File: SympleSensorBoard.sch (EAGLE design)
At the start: 49 parts, among them IC1 STM32F303K8T6, J1 B2B-XH-A_LF__SN_, J10 B3B-XH-A_LF__SN_, J11 B3B-XH-A_LF__SN_, J12 B4B-XH-A_LF__SN_, J13 B4B-XH-A_LF__SN_, J14 B4B-XH-A_LF__SN_, J15 B4B-XH-A_LF__SN_, J16 B2B-XH-A_LF__SN_, J2 B2B-XH-A_LF__SN_, J3 B2B-XH-A_LF__SN_, J4 B2B-XH-A_LF__SN_, J5 B2B-XH-A_LF__SN_, J6 B3B-XH-A_LF__SN_, J7 B3B-XH-A_LF__SN_, J8 B3B-XH-A_LF__SN_, J9 B3B-XH-A_LF__SN_, Y1 CSTCE12M0G55-R0

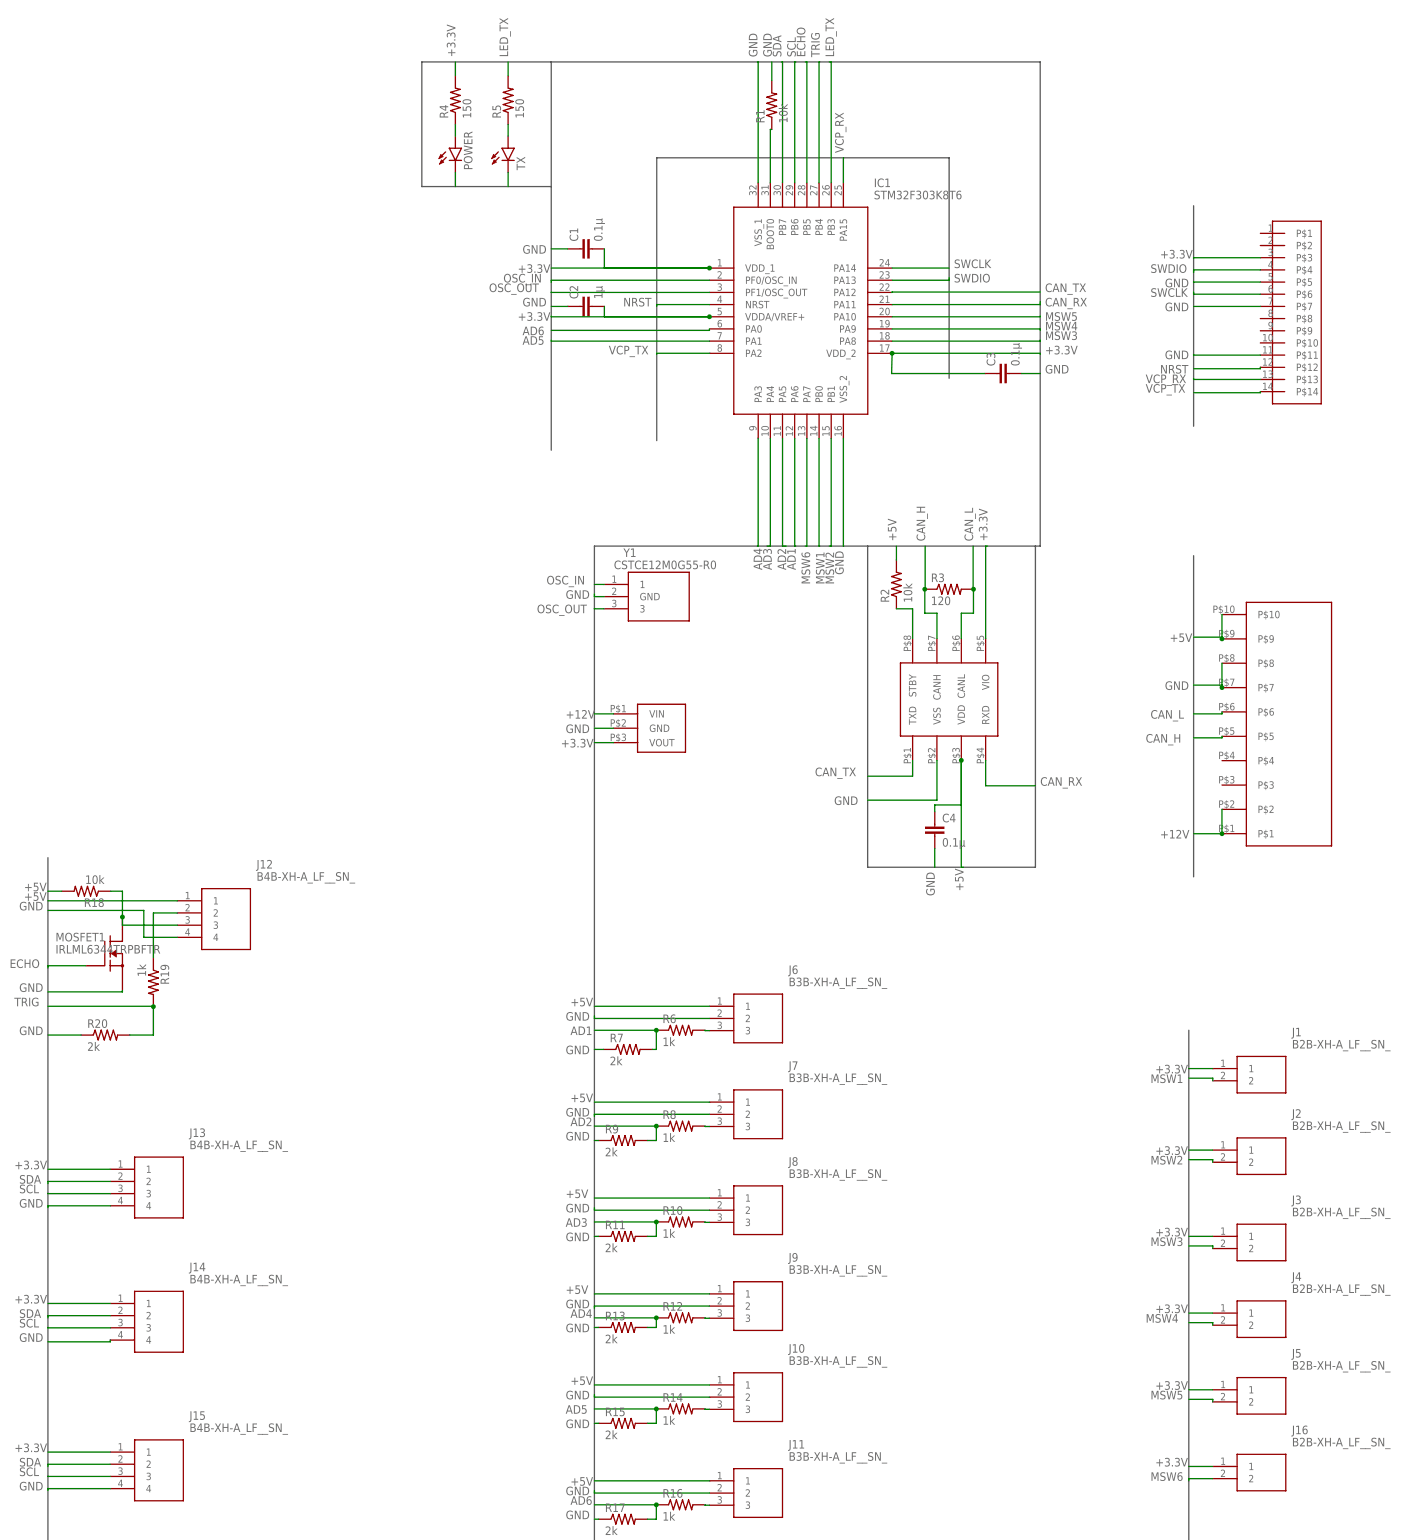
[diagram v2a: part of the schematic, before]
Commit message: コネクタ位置の修正、コネクタ番号を基盤上に表示、部品の再配置、再配線完了。使うセンサはまだ決まっていない。
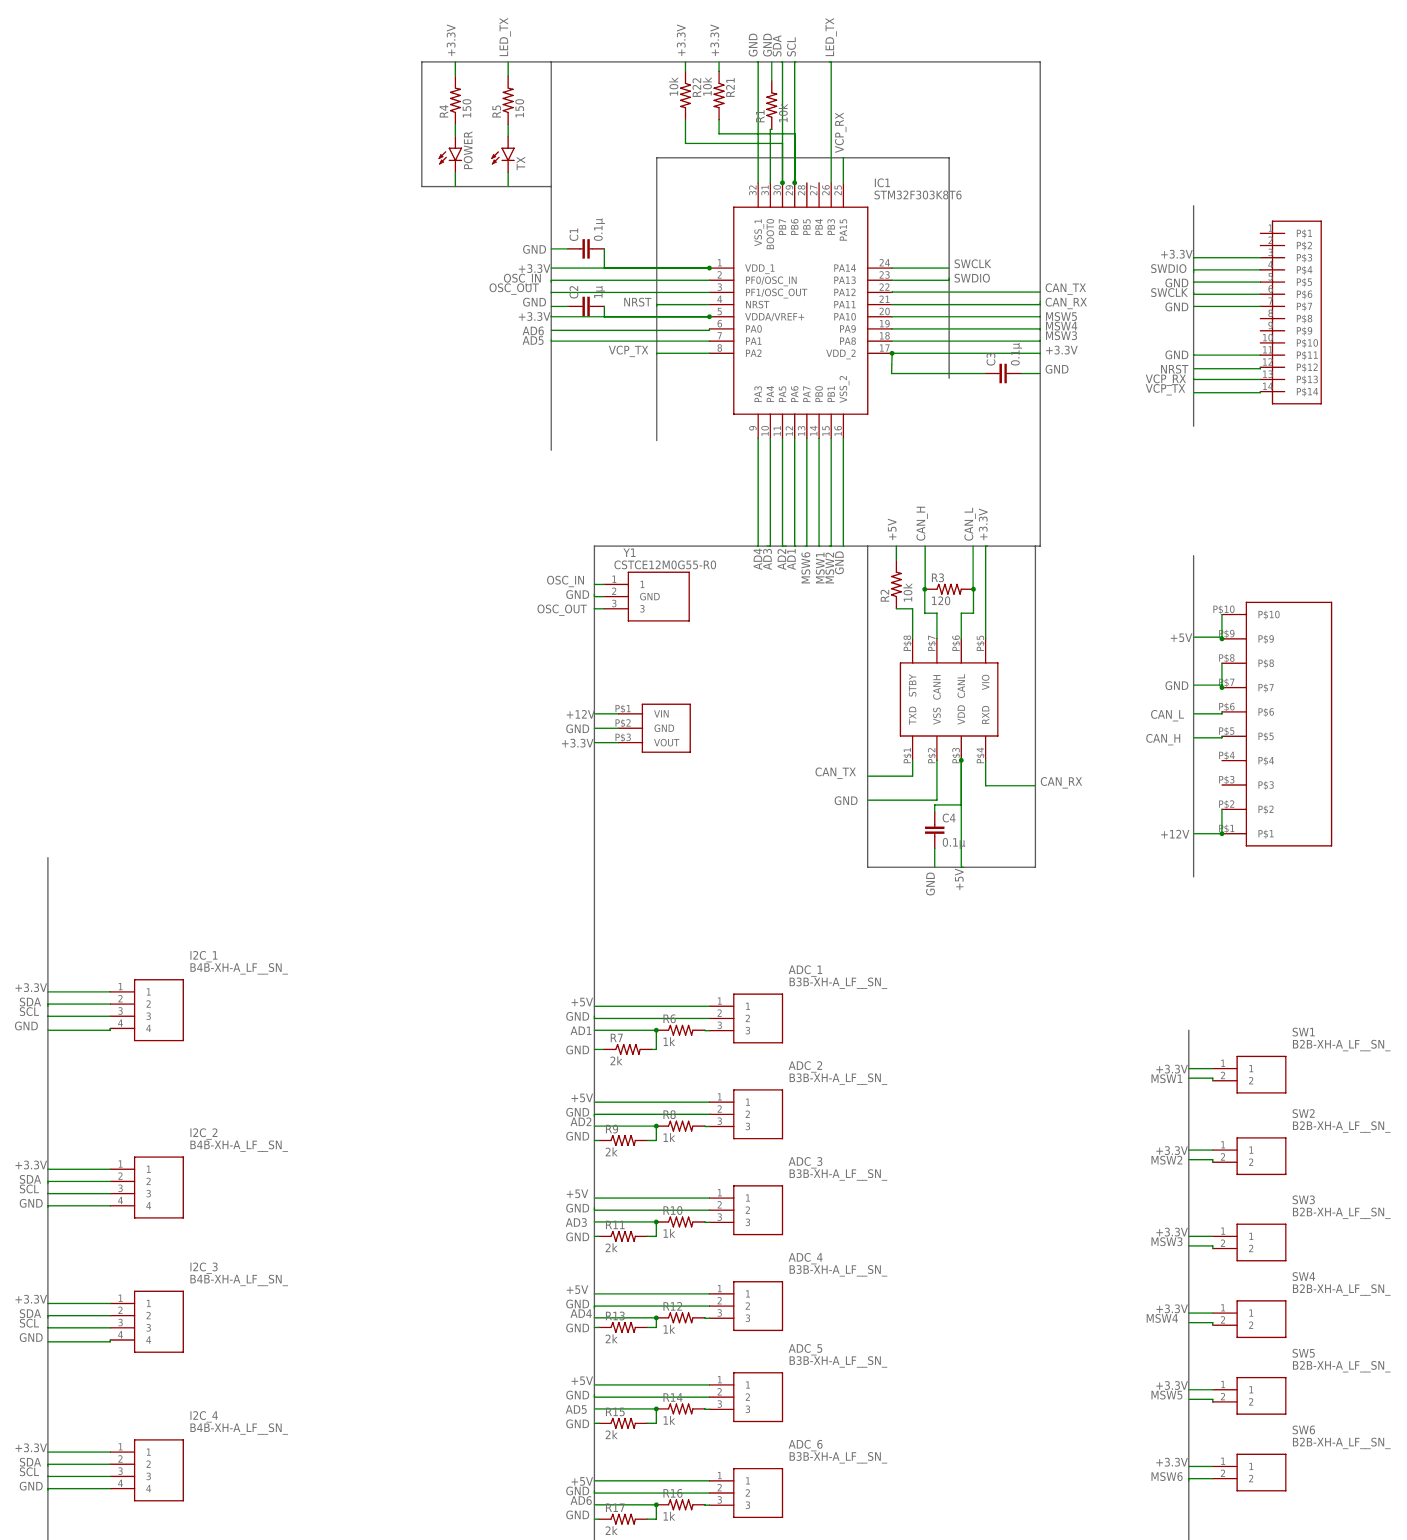
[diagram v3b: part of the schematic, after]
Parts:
- removed J12: B4B-XH-A_LF__SN_, B4B-XH-A_LF__SN_:B4B-XH-A_LF__SN_
- removed MOSFET1: IRLML6344TRPBFTR, mukuchin_transistor_fet_igbt:IRLML6344TRPBFTR
- removed R18: 10k, rcl:R-US_R0603
- removed R19: 1k, rcl:R-US_R0603
- removed R20: 2k, rcl:R-US_R0603
- added I2C_1: B4B-XH-A_LF__SN_, B4B-XH-A_LF__SN_:B4B-XH-A_LF__SN_
- added R21, R22: 10k, rcl:R-US_R0603
- renumbered J1 to SW1, J10 to ADC_5, J11 to ADC_6, J13 to I2C_2, J14 to I2C_3, J15 to I2C_4, J16 to SW6, J2 to SW2, J3 to SW3, J4 to SW4, J5 to SW5, J6 to ADC_1, J7 to ADC_2, J8 to ADC_3, J9 to ADC_4
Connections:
- removed net ECHO: IC1.PB5, MOSFET1.G
- removed net N$11: J12.3, MOSFET1.D, R18.1
- removed net N$13: J12.2, R19.1
- removed net TRIG: IC1.PB4, R19.2, R20.2
- net +3.3V: now also I2C_1.1, R21.1, R22.1
- net +5V: no longer J12.1, R18.2
- net GND: now also I2C_1.4; no longer J12.4, MOSFET1.S, R20.1
- net SCL: now also I2C_1.3, R21.2
- net SDA: now also I2C_1.2, R22.2

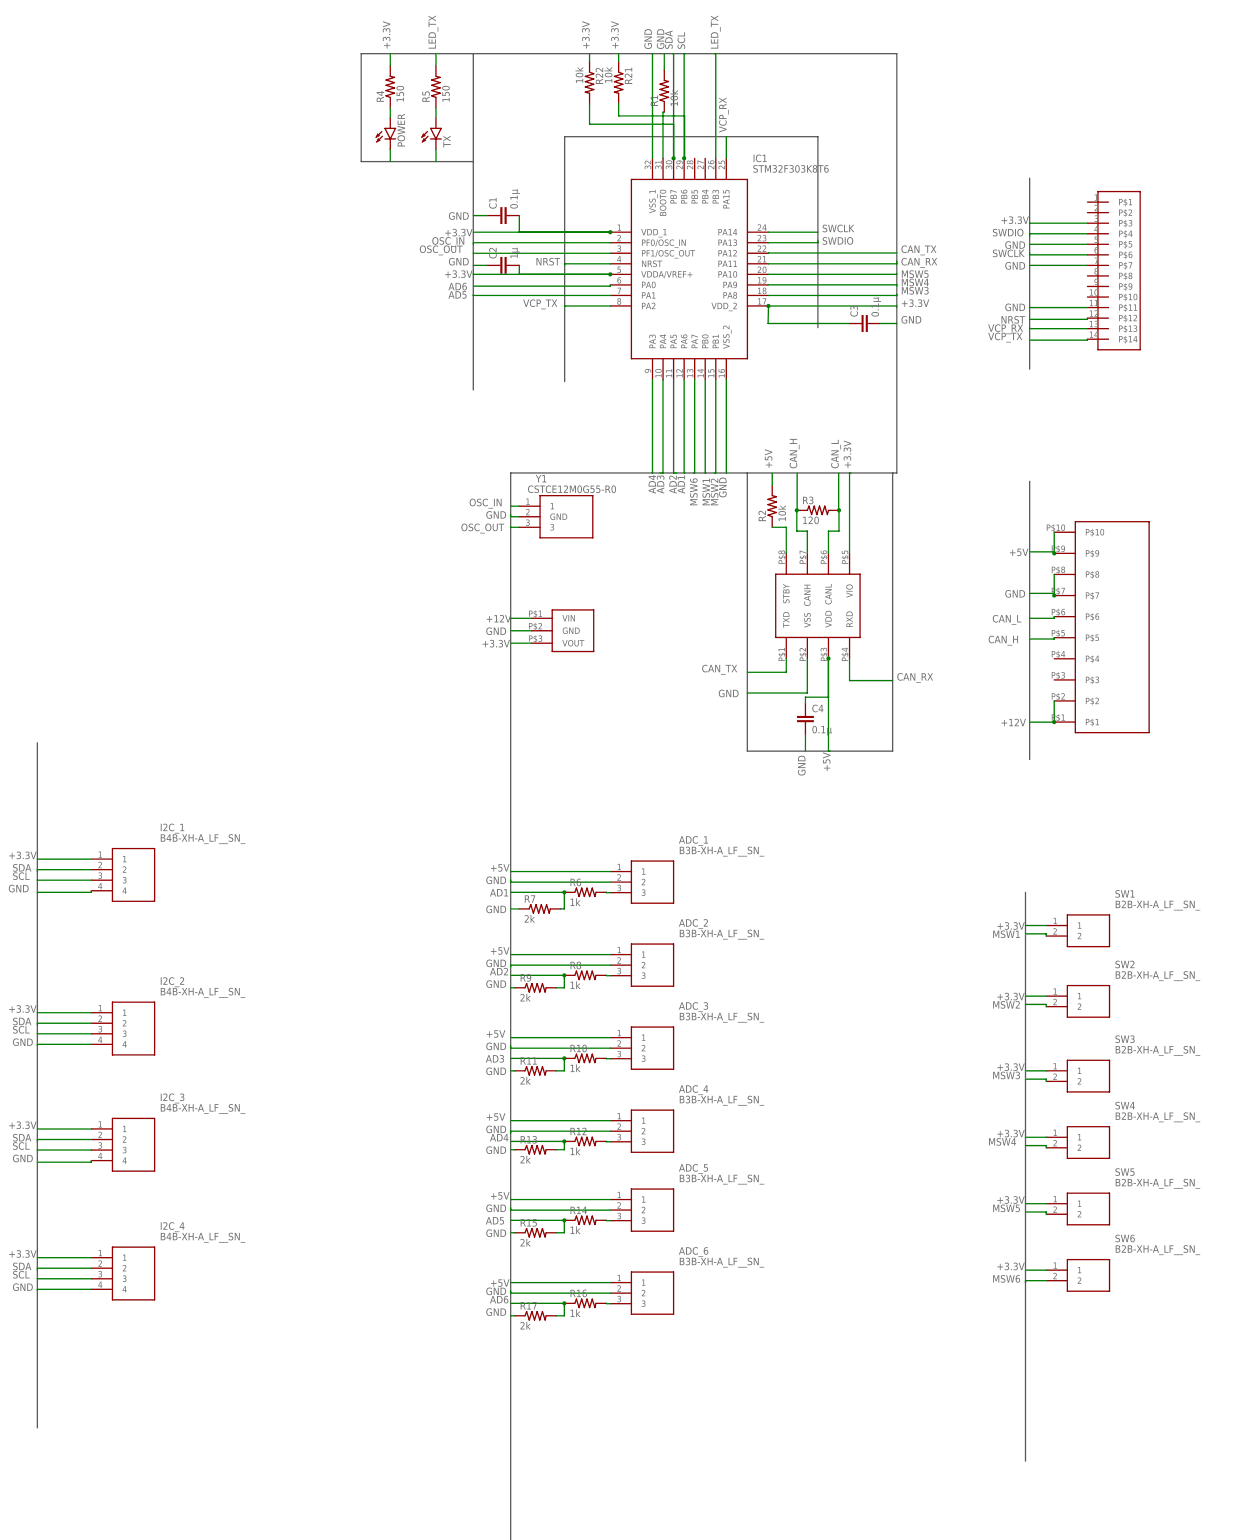
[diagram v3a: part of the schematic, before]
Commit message: I2Cコネクタを全て外した。I2Cは別の基盤で行う。
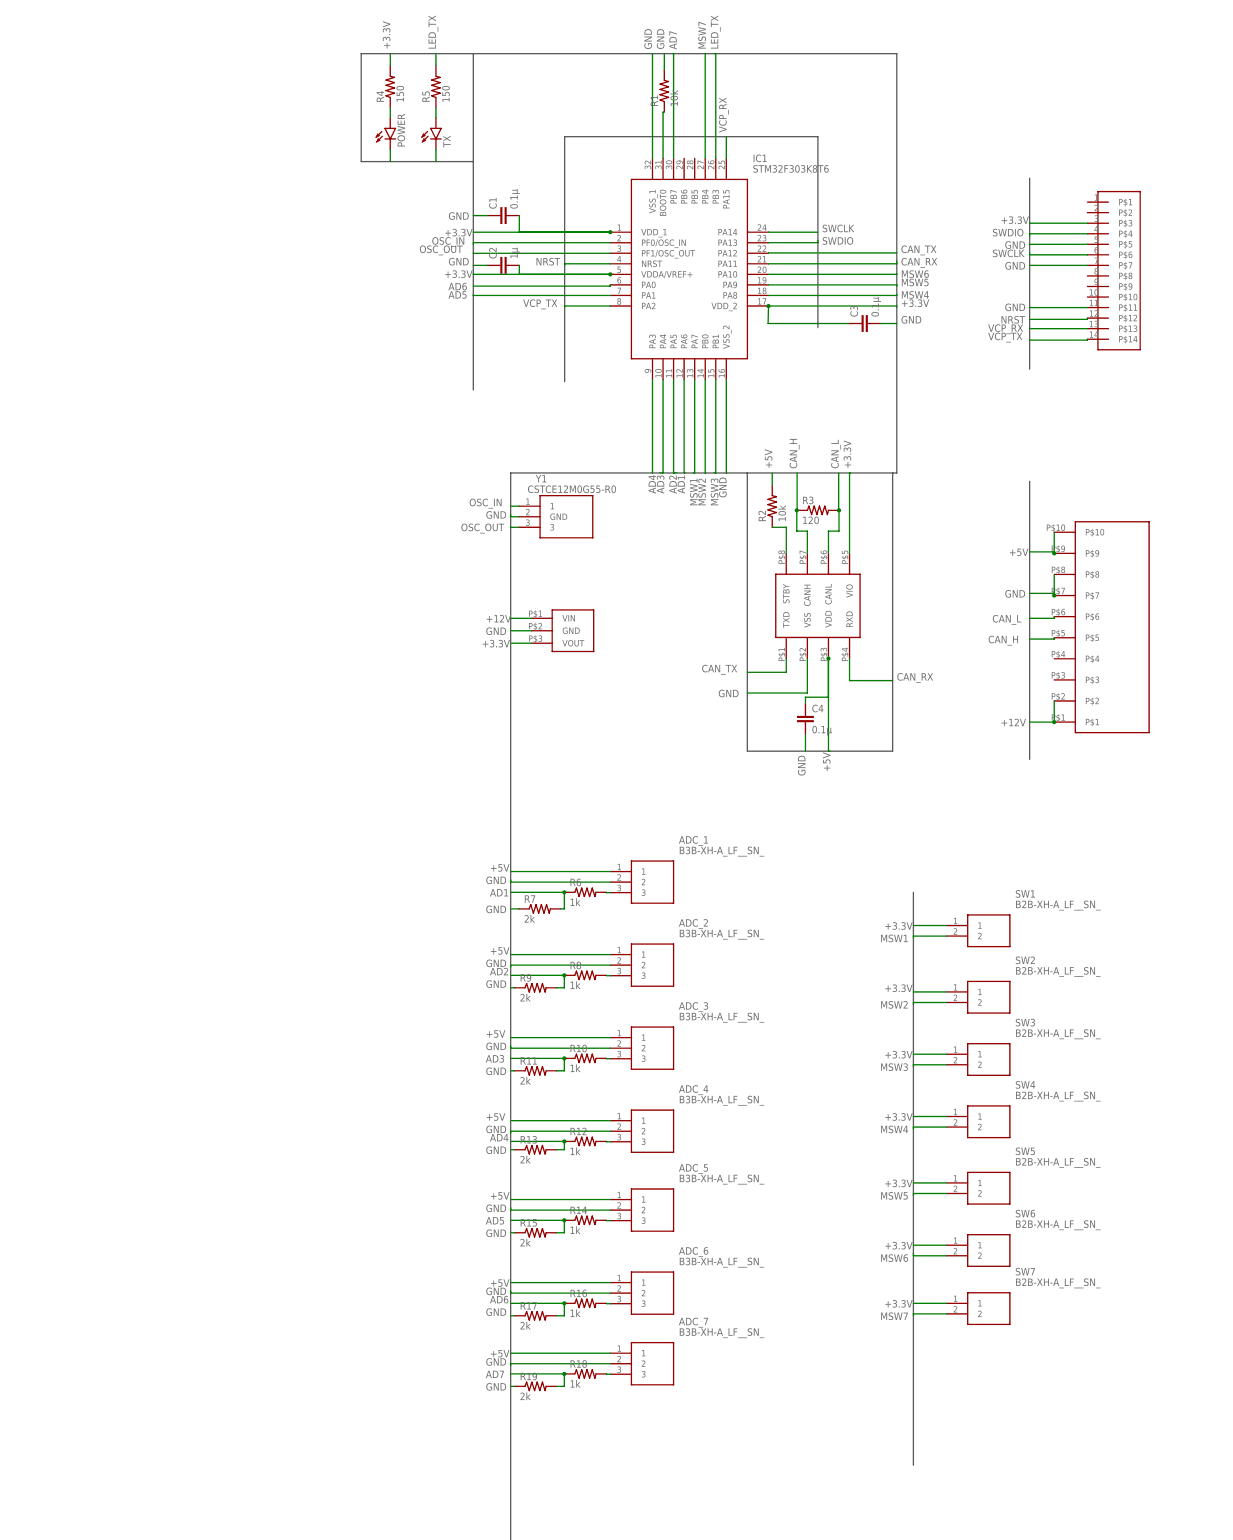
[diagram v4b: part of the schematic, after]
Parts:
- removed I2C_1, I2C_2, I2C_3, I2C_4: B4B-XH-A_LF__SN_, B4B-XH-A_LF__SN_:B4B-XH-A_LF__SN_
- removed R21, R22: 10k, rcl:R-US_R0603
- added ADC_7: B3B-XH-A_LF__SN_, B3B-XH-A_LF__SN_:B3B-XH-A_LF__SN_
- added R18: 1k, rcl:R-US_R0603
- added R19: 2k, rcl:R-US_R0603
- added SW7: B2B-XH-A_LF__SN_, B2B-XH-A_LF__SN_:B2B-XH-A_LF__SN_
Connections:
- removed net SCL: I2C_1.3, I2C_2.3, I2C_3.3, I2C_4.3, IC1.PB6, R21.2
- removed net SDA: I2C_1.2, I2C_2.2, I2C_3.2, I2C_4.2, IC1.PB7, R22.2
- new net AD7: IC1.PB7, R18.1, R19.2
- new net MSW7: IC1.PB4, SW7.2
- new net N$20: ADC_7.3, R18.2
- net +3.3V: now also SW7.1; no longer I2C_1.1, I2C_2.1, I2C_3.1, I2C_4.1, R21.1, R22.1
- net +5V: now also ADC_7.1
- net GND: now also ADC_7.2, R19.1; no longer I2C_1.4, I2C_2.4, I2C_3.4, I2C_4.4
- net MSW1: now also IC1.PA7; no longer IC1.PB0
- net MSW2: now also IC1.PB0; no longer IC1.PB1
- net MSW3: now also IC1.PB1; no longer IC1.PA8
- net MSW4: now also IC1.PA8; no longer IC1.PA9
- net MSW5: now also IC1.PA9; no longer IC1.PA10
- net MSW6: now also IC1.PA10; no longer IC1.PA7
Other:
- moved on the sheet: SW1, SW2, SW3, SW4, SW5, SW6
